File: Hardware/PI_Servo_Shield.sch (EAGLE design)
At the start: 109 parts, among them J1 RASPBERRYPI-40-PIN-GPIO, J19 QWIIC, J20 USB C, J21 Serial, Q1 2N7002PW, Q12 2.5A/30V/105mΩ, Q2 2.5A/30V/105mΩ, Q4 2N7002PW, Q5 2.5A/30V/105mΩ, Q7 2.5A/30V/105mΩ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

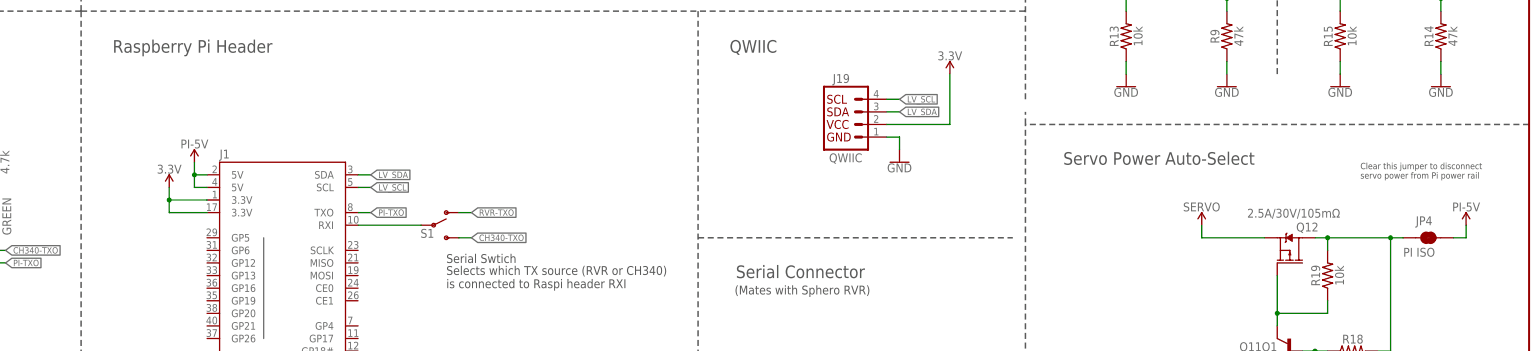
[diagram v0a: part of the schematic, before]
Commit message: Placed all ideal diodes and routed most things
still need a cap and test points placed and routed.
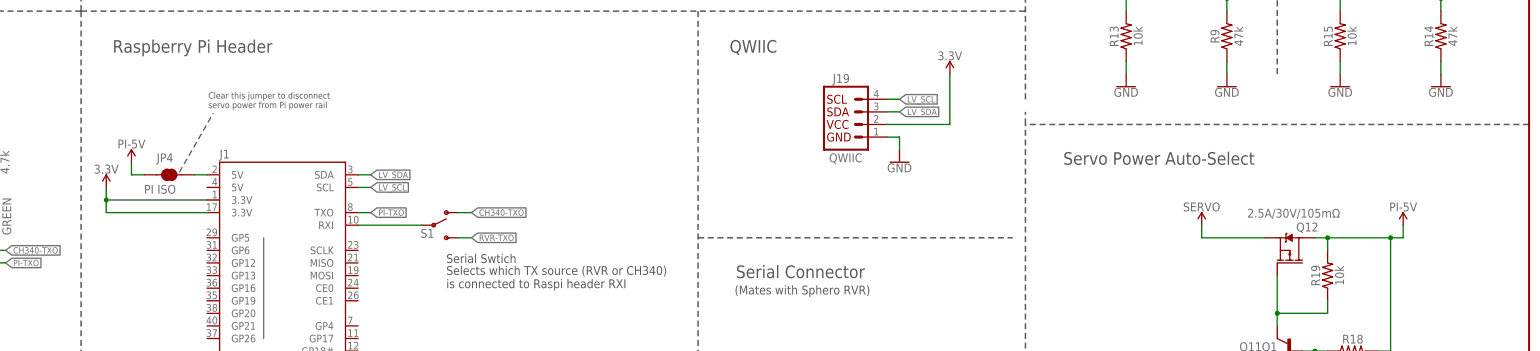
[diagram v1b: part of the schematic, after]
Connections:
- removed net VIN: JP4.2
- net CH340-TXO: now also S1.O; no longer S1.S
- net N$20: now also J1.5V@2, JP4.2; no longer JP4.1, Q12.D, R18.2, R19.2
- net PI-5V: now also JP4.1, Q12.D, R18.2, R19.2; no longer J1.5V@2, J1.5V@4
- net RVR-TXO: now also S1.S; no longer S1.O
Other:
- moved on the sheet: JP4
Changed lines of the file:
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@@
 <part name="RVR-5V" library="SparkFun-PowerSymbols" deviceset="VIN" device="" value="RVR-5V"/>
 <part name="JP4" library="SparkFun-Jumpers" deviceset="JUMPER-SMT_2_NC_TRACE" device="_SILK" value="PI ISO"/>
-<part name="5V1" library="SparkFun-PowerSymbols" deviceset="VIN" device="" value="PI-5V"/>
 <part name="3.3V" library="SparkFun-PowerSymbols" deviceset="VIN" device="" value="3.3V"/>
 <part name="3.3V1" library="SparkFun-PowerSymbols" deviceset="VIN" device="" value="3.3V"/>
@@
 <part name="5V10" library="SparkFun-PowerSymbols" deviceset="VIN" device="" value="PI-5V"/>
 <part name="5V11" library="SparkFun-PowerSymbols" deviceset="VIN" device="" value="PI-5V"/>
+<part name="5V2" library="SparkFun-PowerSymbols" deviceset="VIN" device="" value="PI-5V"/>
 </parts>
 <sheets>
@@
 <text x="7.62" y="271.78" size="2.54" layer="97" font="vector">Servo Connections</text>
 <wire x1="139.7" y1="152.4" x2="139.7" y2="279.4" width="0.3048" layer="97" style="longdash"/>
-<text x="397.764" y="118.618" size="1.27" layer="97" font="vector" ratio="12">Clear this jumper to disconnect
+<text x="165.354" y="132.842" size="1.27" layer="97" font="vector" ratio="12">Clear this jumper to disconnect
 servo power from Pi power rail</text>
 <text x="180.34" y="234.95" size="1.778" layer="97" font="vector">I2C Addr 0x40</text>
@@
 <wire x1="431.8" y1="129.54" x2="330.2" y2="129.54" width="0.3048" layer="97" style="longdash"/>
 <text x="337.82" y="271.272" size="2.54" layer="97" font="vector">Reverse Current Protection</text>
+<wire x1="159.512" y1="119.888" x2="166.37" y2="131.826" width="0.1524" layer="97" style="shortdash"/>
 </plain>
 <instances>
@@
 <attribute name="VALUE" x="294.64" y="78.994" size="1.778" layer="96" font="vector" rot="MR0" align="bottom-center"/>
 </instance>
-<instance part="JP4" gate="G$1" x="411.48" y="106.68" smashed="yes">
-<attribute name="NAME" x="408.94" y="109.22" size="1.778" layer="95" font="vector"/>
-<attribute name="VALUE" x="406.4" y="104.648" size="1.778" layer="96" font="vector" align="top-left"/>
-</instance>
-<instance part="5V1" gate="G$1" x="162.56" y="121.92" smashed="yes" rot="MR0">
-<attribute name="VALUE" x="162.56" y="124.714" size="1.778" layer="96" font="vector" rot="MR0" align="bottom-center"/>
+<instance part="JP4" gate="G$1" x="157.48" y="119.38" smashed="yes">
+<attribute name="NAME" x="154.94" y="121.92" size="1.778" layer="95" font="vector"/>
+<attribute name="VALUE" x="152.4" y="117.348" size="1.778" layer="96" font="vector" align="top-left"/>
 </instance>
 <instance part="3.3V" gate="G$1" x="15.24" y="40.64" smashed="yes" rot="MR0">
@@
 <attribute name="VALUE" x="314.96" y="142.494" size="1.778" layer="96" font="vector" rot="MR0" align="bottom-center"/>
 </instance>
-<instance part="3.3V5" gate="G$1" x="157.48" y="116.84" smashed="yes" rot="MR0">
-<attribute name="VALUE" x="157.48" y="119.634" size="1.778" layer="96" font="vector" rot="MR0" align="bottom-center"/>
+<instance part="3.3V5" gate="G$1" x="144.78" y="116.84" smashed="yes" rot="MR0">
+<attribute name="VALUE" x="144.78" y="119.634" size="1.778" layer="96" font="vector" rot="MR0" align="bottom-center"/>
 </instance>
 <instance part="3.3V6" gate="G$1" x="86.36" y="106.68" smashed="yes" rot="MR0">
@@
 <attribute name="VALUE" x="350.52" y="42.926" size="1.778" layer="96" font="vector" align="top-center"/>
 </instance>
-<instance part="5V8" gate="G$1" x="419.1" y="109.22" smashed="yes" rot="MR0">
-<attribute name="VALUE" x="419.1" y="112.014" size="1.778" layer="96" font="vector" rot="MR0" align="bottom-center"/>
+<instance part="5V8" gate="G$1" x="406.4" y="109.22" smashed="yes" rot="MR0">
+<attribute name="VALUE" x="406.4" y="112.014" size="1.778" layer="96" font="vector" rot="MR0" align="bottom-center"/>
 </instance>
 <instance part="SUPPLY13" gate="G$1" x="365.76" y="109.22" smashed="yes">
@@
 <instance part="5V11" gate="G$1" x="236.22" y="246.38" smashed="yes" rot="MR0">
 <attribute name="VALUE" x="236.22" y="249.174" size="1.778" layer="96" font="vector" rot="MR0" align="bottom-center"/>
+</instance>
+<instance part="5V2" gate="G$1" x="149.86" y="121.92" smashed="yes" rot="MR0">
+<attribute name="VALUE" x="149.86" y="124.714" size="1.778" layer="96" font="vector" rot="MR0" align="bottom-center"/>
 </instance>
 </instances>
@@
 <net name="PI-5V" class="0">
 <segment>
-<pinref part="5V1" gate="G$1" pin="VIN"/>
-<pinref part="J1" gate="G$1" pin="5V@4"/>
-<wire x1="165.1" y1="116.84" x2="162.56" y2="116.84" width="0.1524" layer="91"/>
-<pinref part="J1" gate="G$1" pin="5V@2"/>
-<wire x1="165.1" y1="119.38" x2="162.56" y2="119.38" width="0.1524" layer="91"/>
-<wire x1="162.56" y1="116.84" x2="162.56" y2="119.38" width="0.1524" layer="91"/>
-<junction x="162.56" y="119.38"/>
-<wire x1="162.56" y1="119.38" x2="162.56" y2="121.92" width="0.1524" layer="91"/>
-</segment>
-<segment>
 <pinref part="R1" gate="G$1" pin="2"/>
 <wire x1="241.3" y1="241.3" x2="241.3" y2="243.84" width="0.1524" layer="91"/>
@@
 <pinref part="TP24" gate="G$1" pin="1"/>
 <wire x1="114.3" y1="55.88" x2="111.76" y2="55.88" width="0.1524" layer="91"/>
+</segment>
+<segment>
+<pinref part="5V8" gate="G$1" pin="VIN"/>
+<wire x1="406.4" y1="106.68" x2="406.4" y2="109.22" width="0.1524" layer="91"/>
+<pinref part="Q12" gate="G$1" pin="D"/>
+<wire x1="388.62" y1="106.68" x2="391.16" y2="106.68" width="0.1524" layer="91"/>
+<pinref part="R19" gate="G$1" pin="2"/>
+<wire x1="391.16" y1="106.68" x2="391.16" y2="104.14" width="0.1524" layer="91"/>
+<pinref part="R18" gate="G$1" pin="2"/>
+<wire x1="401.32" y1="83.82" x2="403.86" y2="83.82" width="0.1524" layer="91"/>
+<wire x1="403.86" y1="83.82" x2="403.86" y2="106.68" width="0.1524" layer="91"/>
+<wire x1="403.86" y1="106.68" x2="391.16" y2="106.68" width="0.1524" layer="91"/>
+<junction x="391.16" y="106.68"/>
+<wire x1="406.4" y1="106.68" x2="403.86" y2="106.68" width="0.1524" layer="91"/>
+<junction x="403.86" y="106.68"/>
+</segment>
+<segment>
+<pinref part="5V2" gate="G$1" pin="VIN"/>
+<wire x1="149.86" y1="119.38" x2="149.86" y2="121.92" width="0.1524" layer="91"/>
+<pinref part="JP4" gate="G$1" pin="1"/>
+<wire x1="152.4" y1="119.38" x2="149.86" y2="119.38" width="0.1524" layer="91"/>
 </segment>
 </net>
@@
 <pinref part="J1" gate="G$1" pin="3.3V@17"/>
 <pinref part="J1" gate="G$1" pin="3.3V@1"/>
-<wire x1="157.48" y1="111.76" x2="165.1" y2="111.76" width="0.1524" layer="91"/>
-<wire x1="157.48" y1="114.3" x2="165.1" y2="114.3" width="0.1524" layer="91"/>
-<wire x1="157.48" y1="111.76" x2="157.48" y2="114.3" width="0.1524" layer="91"/>
-<junction x="157.48" y="114.3"/>
-<wire x1="157.48" y1="114.3" x2="157.48" y2="116.84" width="0.1524" layer="91"/>
+<wire x1="144.78" y1="111.76" x2="165.1" y2="111.76" width="0.1524" layer="91"/>
+<wire x1="144.78" y1="114.3" x2="165.1" y2="114.3" width="0.1524" layer="91"/>
+<wire x1="144.78" y1="111.76" x2="144.78" y2="114.3" width="0.1524" layer="91"/>
+<junction x="144.78" y="114.3"/>
+<wire x1="144.78" y1="114.3" x2="144.78" y2="116.84" width="0.1524" layer="91"/>
 </segment>
 <segment>
@@
 </segment>
 <segment>
-<pinref part="S1" gate="1" pin="O"/>
-<wire x1="215.9" y1="111.76" x2="218.44" y2="111.76" width="0.1524" layer="91"/>
-<label x="218.44" y="111.76" size="1.27" layer="95" xref="yes"/>
-</segment>
-<segment>
 <pinref part="TP21" gate="G$1" pin="1"/>
 <wire x1="114.3" y1="38.1" x2="111.76" y2="38.1" width="0.1524" layer="91"/>
 <label x="111.76" y="38.1" size="1.27" layer="95" font="vector" rot="R180" xref="yes"/>
+</segment>
+<segment>
+<wire x1="215.9" y1="106.68" x2="218.44" y2="106.68" width="0.1524" layer="91"/>
+<label x="218.44" y="106.68" size="1.27" layer="95" xref="yes"/>
+<pinref part="S1" gate="1" pin="S"/>
 </segment>
 </net>
@@
 </segment>
 <segment>
-<pinref part="S1" gate="1" pin="S"/>
-<wire x1="215.9" y1="106.68" x2="218.44" y2="106.68" width="0.1524" layer="91"/>
-<label x="218.44" y="106.68" size="1.27" layer="95" xref="yes"/>
-</segment>
-<segment>
 <pinref part="TP23" gate="G$1" pin="1"/>
 <wire x1="114.3" y1="35.56" x2="111.76" y2="35.56" width="0.1524" layer="91"/>
 <label x="111.76" y="35.56" size="1.27" layer="95" rot="R180" xref="yes"/>
 </segment>
-</net>
-<net name="VIN" class="0">
-<segment>
-<pinref part="5V8" gate="G$1" pin="VIN"/>
-<wire x1="419.1" y1="106.68" x2="419.1" y2="109.22" width="0.1524" layer="91"/>
+<segment>
+<wire x1="215.9" y1="111.76" x2="218.44" y2="111.76" width="0.1524" layer="91"/>
+<label x="218.44" y="111.76" size="1.27" layer="95" xref="yes"/>
+<pinref part="S1" gate="1" pin="O"/>
+</segment>
+</net>
+<net name="N$20" class="0">
+<segment>
+<pinref part="J1" gate="G$1" pin="5V@2"/>
 <pinref part="JP4" gate="G$1" pin="2"/>
-<wire x1="416.56" y1="106.68" x2="419.1" y2="106.68" width="0.1524" layer="91"/>
-</segment>
-</net>
-<net name="N$20" class="0">
-<segment>
-<pinref part="Q12" gate="G$1" pin="D"/>
-<wire x1="388.62" y1="106.68" x2="391.16" y2="106.68" width="0.1524" layer="91"/>
-<pinref part="R19" gate="G$1" pin="2"/>
-<wire x1="391.16" y1="106.68" x2="391.16" y2="104.14" width="0.1524" layer="91"/>
-<pinref part="R18" gate="G$1" pin="2"/>
-<wire x1="401.32" y1="83.82" x2="403.86" y2="83.82" width="0.1524" layer="91"/>
-<wire x1="403.86" y1="83.82" x2="403.86" y2="106.68" width="0.1524" layer="91"/>
-<wire x1="403.86" y1="106.68" x2="391.16" y2="106.68" width="0.1524" layer="91"/>
-<junction x="391.16" y="106.68"/>
-<pinref part="JP4" gate="G$1" pin="1"/>
-<wire x1="403.86" y1="106.68" x2="406.4" y2="106.68" width="0.1524" layer="91"/>
-<junction x="403.86" y="106.68"/>
-</segment>
-</net>
+<wire x1="165.1" y1="119.38" x2="162.56" y2="119.38" width="0.1524" layer="91"/>
+</segment>
+</net>

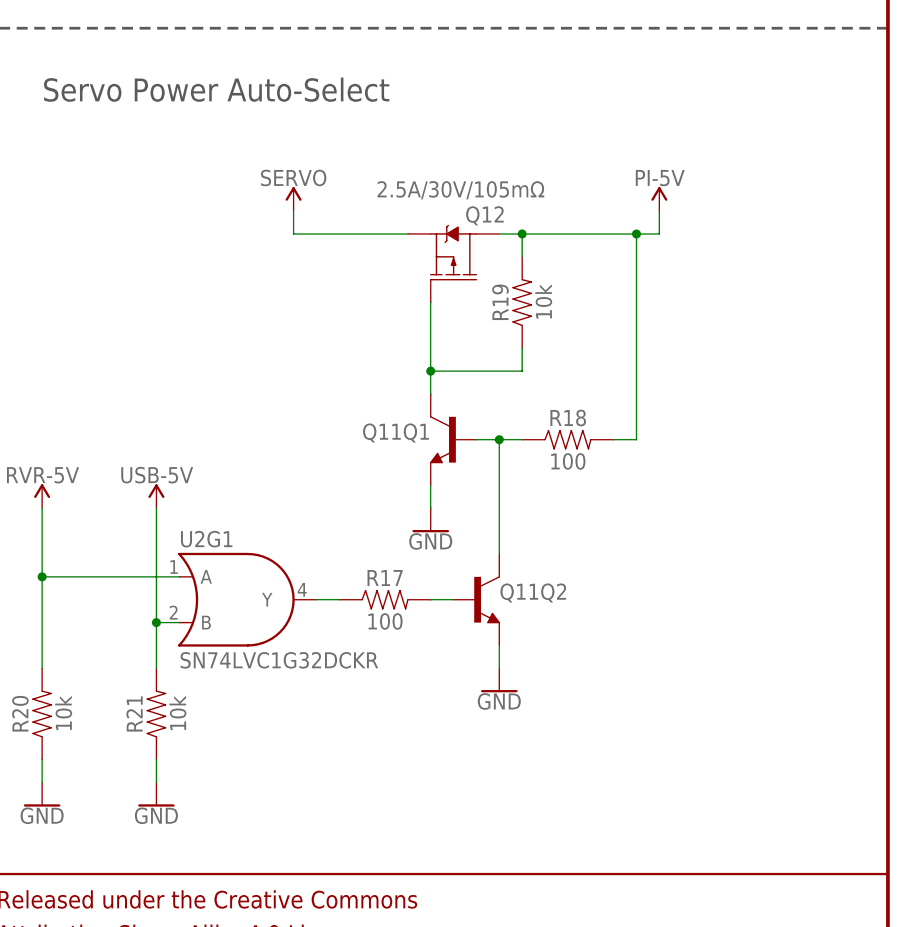
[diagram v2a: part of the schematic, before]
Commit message: Corrected package on OR gate
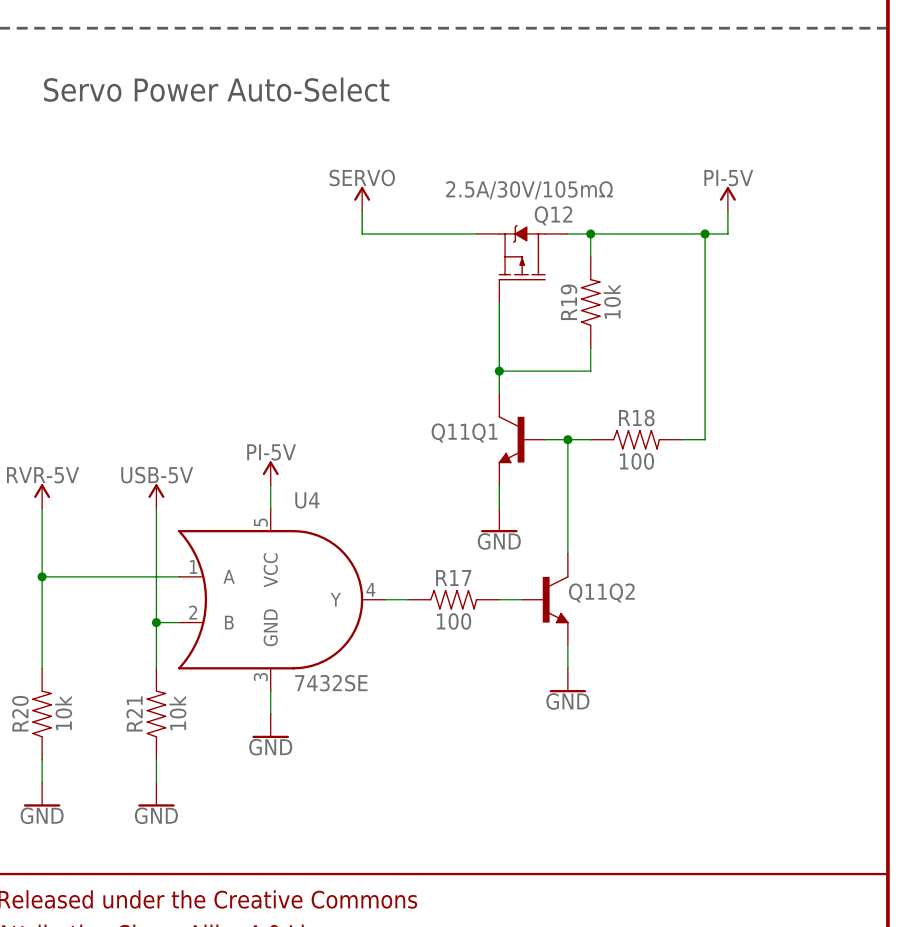
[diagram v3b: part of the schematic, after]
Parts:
- removed U2: SN74LVC1G32DCKR, SparkFun-IC-Logic:74LVC32DBV
- added U4: 7432SE, SparkFun:7432SE
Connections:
- net GND: now also U4.GND
- net N$17: now also U4.Y; no longer U2G1.Y
- net PI-5V: now also U4.VCC
- net RVR-5V: now also U4.A; no longer U2G1.A
- net USB-5V: now also U4.B; no longer U2G1.B
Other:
- moved on the sheet: Q11Q1, Q11Q2, Q12, R17, R18, R19
